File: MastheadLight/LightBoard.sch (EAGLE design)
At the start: 6 parts

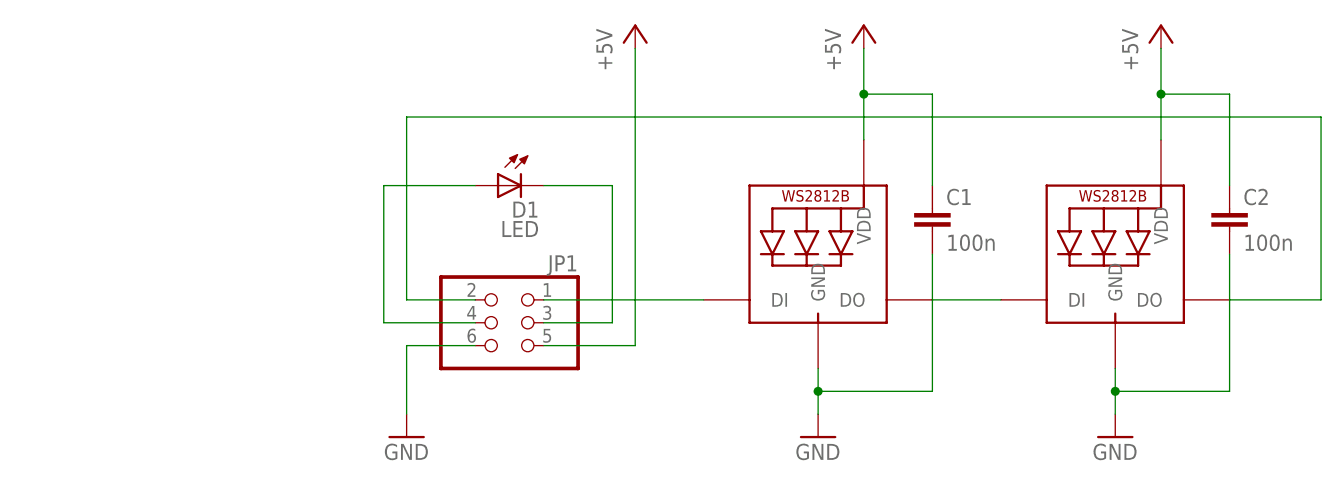
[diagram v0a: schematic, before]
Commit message: Switched the light board to the proper six-pin WS2812B footprint.
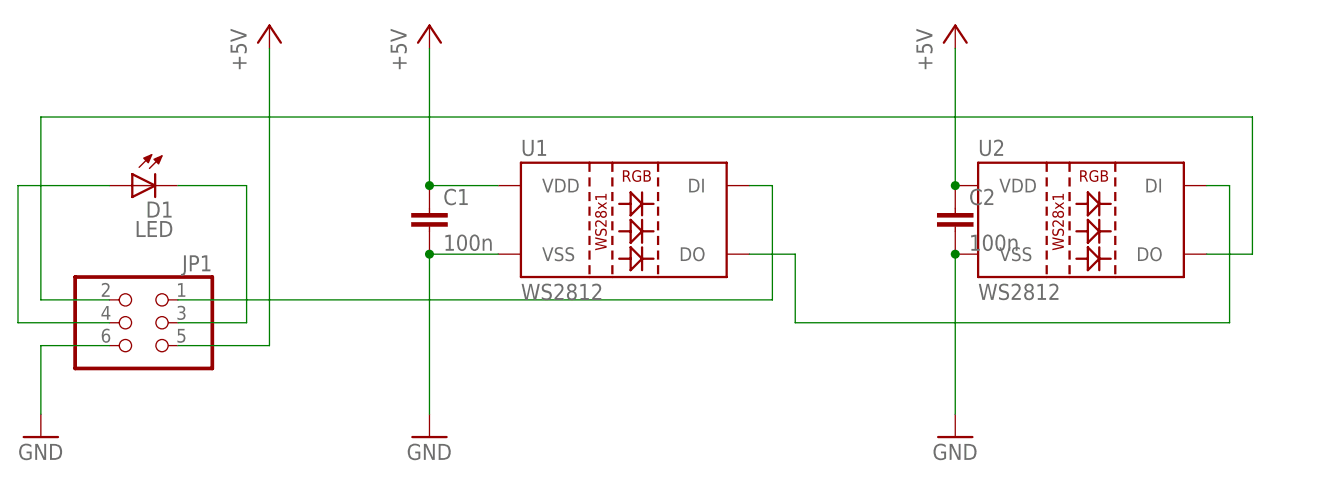
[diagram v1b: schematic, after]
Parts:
- removed LED1, LED2: WS2812B5050, adafruit:WS2812B5050
- added U1, U2: WS2812, SparkFun-LED:WS2812"
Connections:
- net +5V: now also U1.VDD, U2.VDD; no longer LED1.VDD, LED2.VDD
- net GND: now also U1.VSS, U2.VSS; no longer LED1.GND, LED2.GND
- net N$1: now also U1.DO, U2.DI; no longer LED1.DO, LED2.DI
- net N$2: now also U1.DI; no longer LED1.DI
- net N$3: now also U2.DO; no longer LED2.DO
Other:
- moved on the sheet: C1, C2, D1, JP1

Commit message: As per Dec 2019 board orders
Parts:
- removed U1, U2: WS2812, SparkFun-LED:WS2812"
- added D2, D3: WS2812B, SparkFun-LED:WS2812B
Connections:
- net +5V: now also D2.VDD, D3.VDD; no longer U1.VDD, U2.VDD
- net GND: now also D2.VSS, D3.VSS; no longer U1.VSS, U2.VSS
- net N$1: now also D2.DO, D3.DI; no longer U1.DO, U2.DI
- net N$2: now also D2.DI; no longer U1.DI
- net N$3: now also D3.DO; no longer U2.DO
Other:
- moved on the sheet: C2
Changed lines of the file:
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@@
 <?xml version="1.0" encoding="utf-8"?>
 <!DOCTYPE eagle SYSTEM "eagle.dtd">
-<eagle version="8.5.0">
+<eagle version="9.3.2">
 <drawing>
 <settings>
@@
 <layers>
 <layer number="1" name="Top" color="4" fill="1" visible="no" active="no"/>
+<layer number="2" name="Route2" color="1" fill="3" visible="no" active="no"/>
+<layer number="15" name="Route15" color="4" fill="6" visible="no" active="no"/>
 <layer number="16" name="Bottom" color="1" fill="1" visible="no" active="no"/>
 <layer number="17" name="Pads" color="2" fill="1" visible="no" active="no"/>
@@
 <part name="C1" library="resistor" library_urn="urn:adsk.eagle:library:348" deviceset="C-EU" device="C0603" package3d_urn="urn:adsk.eagle:package:26138/1" value="100n"/>
 <part name="C2" library="resistor" library_urn="urn:adsk.eagle:library:348" deviceset="C-EU" device="C0603" package3d_urn="urn:adsk.eagle:package:26138/1" value="100n"/>
-<part name="U1" library="SparkFun-LED" library_urn="urn:adsk.eagle:library:529" deviceset="WS2812" device="&quot;" package3d_urn="urn:adsk.eagle:package:39366/1" value="WS2812"/>
-<part name="U2" library="SparkFun-LED" library_urn="urn:adsk.eagle:library:529" deviceset="WS2812" device="&quot;" package3d_urn="urn:adsk.eagle:package:39366/1" value="WS2812"/>
+<part name="D2" library="SparkFun-LED" library_urn="urn:adsk.eagle:library:529" deviceset="WS2812B" device="" package3d_urn="urn:adsk.eagle:package:39369/1" value="WS2812B"/>
+<part name="D3" library="SparkFun-LED" library_urn="urn:adsk.eagle:library:529" deviceset="WS2812B" device="" package3d_urn="urn:adsk.eagle:package:39369/1" value="WS2812B"/>
 </parts>
 <sheets>
@@
 </plain>
 <instances>
-<instance part="FRAME1" gate="G$1" x="0" y="0"/>
-<instance part="FRAME1" gate="G$2" x="172.72" y="0"/>
-<instance part="D1" gate="G$1" x="101.6" y="116.84" rot="MR270"/>
-<instance part="GND1" gate="1" x="134.62" y="88.9"/>
-<instance part="GND2" gate="1" x="193.04" y="88.9"/>
-<instance part="P+1" gate="1" x="134.62" y="134.62"/>
-<instance part="P+2" gate="1" x="193.04" y="134.62"/>
-<instance part="JP1" gate="A" x="104.14" y="101.6" rot="MR0"/>
-<instance part="GND3" gate="1" x="91.44" y="88.9"/>
-<instance part="P+3" gate="1" x="116.84" y="134.62"/>
-<instance part="C1" gate="G$1" x="134.62" y="114.3"/>
-<instance part="C2" gate="G$1" x="193.04" y="114.3"/>
-<instance part="U1" gate="U1" x="157.48" y="111.76"/>
-<instance part="U2" gate="U1" x="208.28" y="111.76"/>
+<instance part="FRAME1" gate="G$1" x="0" y="0" smashed="yes"/>
+<instance part="FRAME1" gate="G$2" x="172.72" y="0" smashed="yes">
+<attribute name="LAST_DATE_TIME" x="185.42" y="1.27" size="2.54" layer="94"/>
+<attribute name="SHEET" x="259.08" y="1.27" size="2.54" layer="94"/>
+<attribute name="DRAWING_NAME" x="190.5" y="19.05" size="2.54" layer="94"/>
+</instance>
+<instance part="D1" gate="G$1" x="101.6" y="116.84" smashed="yes" rot="MR270">
+<attribute name="NAME" x="106.172" y="113.284" size="1.778" layer="95" rot="MR0"/>
+<attribute name="VALUE" x="106.172" y="111.125" size="1.778" layer="96" rot="MR0"/>
+</instance>
+<instance part="GND1" gate="1" x="134.62" y="88.9" smashed="yes">
+<attribute name="VALUE" x="132.08" y="86.36" size="1.778" layer="96"/>
+</instance>
+<instance part="GND2" gate="1" x="185.42" y="88.9" smashed="yes">
+<attribute name="VALUE" x="182.88" y="86.36" size="1.778" layer="96"/>
+</instance>
+<instance part="P+1" gate="1" x="134.62" y="134.62" smashed="yes">
+<attribute name="VALUE" x="132.08" y="129.54" size="1.778" layer="96" rot="R90"/>
+</instance>
+<instance part="P+2" gate="1" x="185.42" y="134.62" smashed="yes">
+<attribute name="VALUE" x="182.88" y="129.54" size="1.778" layer="96" rot="R90"/>
+</instance>
+<instance part="JP1" gate="A" x="104.14" y="101.6" smashed="yes" rot="MR0">
+<attribute name="NAME" x="110.49" y="107.315" size="1.778" layer="95" rot="MR0"/>
+<attribute name="VALUE" x="110.49" y="93.98" size="1.778" layer="96" rot="MR0"/>
+</instance>
+<instance part="GND3" gate="1" x="91.44" y="88.9" smashed="yes">
+<attribute name="VALUE" x="88.9" y="86.36" size="1.778" layer="96"/>
+</instance>
+<instance part="P+3" gate="1" x="116.84" y="134.62" smashed="yes">
+<attribute name="VALUE" x="114.3" y="129.54" size="1.778" layer="96" rot="R90"/>
+</instance>
+<instance part="C1" gate="G$1" x="134.62" y="114.3" smashed="yes">
+<attribute name="NAME" x="136.144" y="114.681" size="1.778" layer="95"/>
+<attribute name="VALUE" x="136.144" y="109.601" size="1.778" layer="96"/>
+</instance>
+<instance part="C2" gate="G$1" x="185.42" y="114.3" smashed="yes">
+<attribute name="NAME" x="186.944" y="114.681" size="1.778" layer="95"/>
+<attribute name="VALUE" x="186.944" y="109.601" size="1.778" layer="96"/>
+</instance>
+<instance part="D2" gate="G$1" x="157.48" y="111.76" smashed="yes">
+<attribute name="NAME" x="144.78" y="120.142" size="1.778" layer="95"/>
+<attribute name="VALUE" x="144.78" y="104.14" size="1.778" layer="95"/>
+</instance>
+<instance part="D3" gate="G$1" x="208.28" y="111.76" smashed="yes">
+<attribute name="NAME" x="195.58" y="120.142" size="1.778" layer="95"/>
+<attribute name="VALUE" x="195.58" y="104.14" size="1.778" layer="95"/>
+</instance>
 </instances>
 <busses>
@@
 <pinref part="C1" gate="G$1" pin="2"/>
 <wire x1="134.62" y1="91.44" x2="134.62" y2="109.22" width="0.1524" layer="91"/>
-<pinref part="U1" gate="U1" pin="VSS"/>
 <wire x1="142.24" y1="109.22" x2="134.62" y2="109.22" width="0.1524" layer="91"/>
 <junction x="134.62" y="109.22"/>
+<pinref part="D2" gate="G$1" pin="VSS"/>
 </segment>
 <segment>
 <pinref part="GND2" gate="1" pin="GND"/>
 <pinref part="C2" gate="G$1" pin="2"/>
-<wire x1="193.04" y1="91.44" x2="193.04" y2="109.22" width="0.1524" layer="91"/>
-<pinref part="U2" gate="U1" pin="VSS"/>
-<junction x="193.04" y="109.22"/>
+<wire x1="185.42" y1="91.44" x2="185.42" y2="109.22" width="0.1524" layer="91"/>
+<junction x="185.42" y="109.22"/>
+<wire x1="185.42" y1="109.22" x2="193.04" y2="109.22" width="0.1524" layer="91"/>
+<pinref part="D3" gate="G$1" pin="VSS"/>
 </segment>
 <segment>
@@
 <pinref part="P+1" gate="1" pin="+5V"/>
 <pinref part="C1" gate="G$1" pin="1"/>
-<pinref part="U1" gate="U1" pin="VDD"/>
 <wire x1="142.24" y1="116.84" x2="134.62" y2="116.84" width="0.1524" layer="91"/>
 <wire x1="134.62" y1="116.84" x2="134.62" y2="132.08" width="0.1524" layer="91"/>
 <junction x="134.62" y="116.84"/>
+<pinref part="D2" gate="G$1" pin="VDD"/>
 </segment>
 <segment>
 <pinref part="P+2" gate="1" pin="+5V"/>
 <pinref part="C2" gate="G$1" pin="1"/>
-<wire x1="193.04" y1="132.08" x2="193.04" y2="116.84" width="0.1524" layer="91"/>
-<pinref part="U2" gate="U1" pin="VDD"/>
-<junction x="193.04" y="116.84"/>
+<wire x1="185.42" y1="132.08" x2="185.42" y2="116.84" width="0.1524" layer="91"/>
+<junction x="185.42" y="116.84"/>
+<wire x1="185.42" y1="116.84" x2="193.04" y2="116.84" width="0.1524" layer="91"/>
+<pinref part="D3" gate="G$1" pin="VDD"/>
 </segment>
 <segment>
@@
 <wire x1="106.68" y1="104.14" x2="172.72" y2="104.14" width="0.1524" layer="91"/>
 <wire x1="172.72" y1="104.14" x2="172.72" y2="116.84" width="0.1524" layer="91"/>
-<pinref part="U1" gate="U1" pin="DI"/>
 <wire x1="172.72" y1="116.84" x2="170.18" y2="116.84" width="0.1524" layer="91"/>
+<pinref part="D2" gate="G$1" pin="DI"/>
 </segment>
 </net>
@@
 <wire x1="91.44" y1="124.46" x2="226.06" y2="124.46" width="0.1524" layer="91"/>
 <wire x1="226.06" y1="124.46" x2="226.06" y2="109.22" width="0.1524" layer="91"/>
-<pinref part="U2" gate="U1" pin="DO"/>
 <wire x1="220.98" y1="109.22" x2="226.06" y2="109.22" width="0.1524" layer="91"/>
+<pinref part="D3" gate="G$1" pin="DO"/>
 </segment>
 </net>
@@
 <net name="N$1" class="0">
 <segment>
-<pinref part="U1" gate="U1" pin="DO"/>
 <wire x1="170.18" y1="109.22" x2="175.26" y2="109.22" width="0.1524" layer="91"/>
 <wire x1="175.26" y1="109.22" x2="175.26" y2="101.6" width="0.1524" layer="91"/>
 <wire x1="175.26" y1="101.6" x2="223.52" y2="101.6" width="0.1524" layer="91"/>
 <wire x1="223.52" y1="101.6" x2="223.52" y2="116.84" width="0.1524" layer="91"/>
-<pinref part="U2" gate="U1" pin="DI"/>
 <wire x1="223.52" y1="116.84" x2="220.98" y2="116.84" width="0.1524" layer="91"/>
-</segment>
-</net>
+<pinref part="D2" gate="G$1" pin="DO"/>
+<pinref part="D3" gate="G$1" pin="DI"/>
+</segment>
+</net>
